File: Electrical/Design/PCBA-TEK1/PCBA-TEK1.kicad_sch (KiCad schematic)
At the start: 0 parts

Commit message: SUKU sync
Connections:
- no-connect marks 1 -> 11
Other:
- added sheet UI_DISPLAY (UI_DISPLAY.kicad_sch)
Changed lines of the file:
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@@
   (junction (at 213.36 185.42) (diameter 0) (color 0 0 0 0)
   )
+  (no_connect (at 208.28 147.32))
+  (no_connect (at 208.28 165.1))
+  (no_connect (at 208.28 157.48))
+  (no_connect (at 208.28 134.62))
+  (no_connect (at 208.28 160.02))
   (no_connect (at 208.28 111.76))
+  (no_connect (at 208.28 142.24))
+  (no_connect (at 208.28 137.16))
+  (no_connect (at 208.28 129.54))
+  (no_connect (at 208.28 139.7))
+  (no_connect (at 208.28 162.56))
   (wire (pts (xy 175.26 203.2) (xy 170.18 203.2))
     (stroke (width 0) (type default))
@@
     (stroke (width 0) (type default))
   )
+  (wire (pts (xy 203.2 147.32) (xy 208.28 147.32))
+    (stroke (width 0) (type default))
+  )
   (wire (pts (xy 175.26 198.12) (xy 170.18 198.12))
     (stroke (width 0) (type default))
@@
     (stroke (width 0) (type default))
   )
+  (wire (pts (xy 203.2 162.56) (xy 208.28 162.56))
+    (stroke (width 0) (type default))
+  )
   (wire (pts (xy 175.26 220.98) (xy 170.18 220.98))
     (stroke (width 0) (type default))
@@
     (stroke (width 0) (type default))
   )
+  (wire (pts (xy 203.2 129.54) (xy 208.28 129.54))
+    (stroke (width 0) (type default))
+  )
+  (wire (pts (xy 203.2 157.48) (xy 208.28 157.48))
+    (stroke (width 0) (type default))
+  )
+  (wire (pts (xy 203.2 134.62) (xy 208.28 134.62))
+    (stroke (width 0) (type default))
+  )
   (wire (pts (xy 175.26 193.04) (xy 170.18 193.04))
     (stroke (width 0) (type default))
@@
     (stroke (width 0) (type default))
   )
+  (wire (pts (xy 203.2 165.1) (xy 208.28 165.1))
+    (stroke (width 0) (type default))
+  )
   (wire (pts (xy 213.36 185.42) (xy 215.9 185.42))
     (stroke (width 0) (type default))
@@
     (stroke (width 0) (type default))
   )
+  (wire (pts (xy 203.2 142.24) (xy 208.28 142.24))
+    (stroke (width 0) (type default))
+  )
   (wire (pts (xy 215.9 187.96) (xy 213.36 187.96))
     (stroke (width 0) (type default))
@@
     (stroke (width 0) (type default))
   )
+  (wire (pts (xy 203.2 160.02) (xy 208.28 160.02))
+    (stroke (width 0) (type default))
+  )
+  (wire (pts (xy 203.2 139.7) (xy 208.28 139.7))
+    (stroke (width 0) (type default))
+  )
   (wire (pts (xy 200.66 198.12) (xy 215.9 198.12))
     (stroke (width 0) (type default))
   )
   (wire (pts (xy 127 193.04) (xy 132.08 193.04))
+    (stroke (width 0) (type default))
+  )
+  (wire (pts (xy 203.2 137.16) (xy 208.28 137.16))
     (stroke (width 0) (type default))
   )
@@
       )
     )
+  )
+  (sheet (at 177.8 127) (size 25.4 40.64) (fields_autoplaced)
+    (stroke (width 0.1524) (type solid))
+    (fill (color 0 0 0 0.0000))
+    (property "Sheetname" "UI_DISPLAY" (at 177.8 126.2884 0)
+      (effects (font (size 1.27 1.27)) (justify left bottom))
+    )
+    (property "Sheetfile" "UI_DISPLAY.kicad_sch" (at 177.8 168.2246 0)
+      (effects (font (size 1.27 1.27)) (justify left top))
+    )
+    (pin "~{RESET}" input (at 203.2 147.32 0)
+      (effects (font (size 1.27 1.27)) (justify right))
+    )
+    (pin "~{BACKLIGHT}" passive (at 203.2 129.54 0)
+      (effects (font (size 1.27 1.27)) (justify right))
+    )
+    (pin "~{CS}" input (at 203.2 134.62 0)
+      (effects (font (size 1.27 1.27)) (justify right))
+    )
+    (pin "D{slash}~{C}" input (at 203.2 137.16 0)
+      (effects (font (size 1.27 1.27)) (justify right))
+    )
+    (pin "SDIO" input (at 203.2 139.7 0)
+      (effects (font (size 1.27 1.27)) (justify right))
+    )
+    (pin "SCLK" input (at 203.2 142.24 0)
+      (effects (font (size 1.27 1.27)) (justify right))
+    )
+    (pin "BTN_1" output (at 203.2 160.02 0)
+      (effects (font (size 1.27 1.27)) (justify right))
+    )
+    (pin "BTN_0" output (at 203.2 157.48 0)
+      (effects (font (size 1.27 1.27)) (justify right))
+    )
+    (pin "BTN_3" output (at 203.2 162.56 0)
+      (effects (font (size 1.27 1.27)) (justify right))
+    )
+    (pin "BTN_2" output (at 203.2 165.1 0)
+      (effects (font (size 1.27 1.27)) (justify right))
+    )
+    (instances
+      (project "PCBA-TEK1"
+        (path "/e5217a0c-7f55-4c30-adda-7f8d95709d1b" (page "11"))
+      )
+    )

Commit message: SUKU layout finished
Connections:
- no-connect marks 11 -> 1
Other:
- sheet UI_POT renamed UI_POT_BTN
- sheet UI_DISPLAY ports: added none; removed BTN_0, BTN_1, BTN_2, BTN_3
- sheet UI_POT_BTN: file UI_POT.kicad_sch -> UI_POT_BTN.kicad_sch

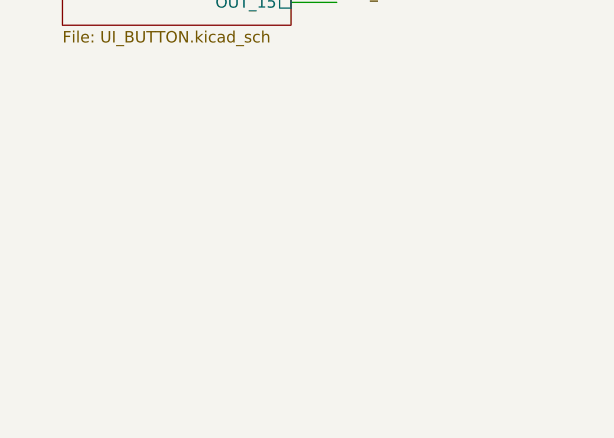
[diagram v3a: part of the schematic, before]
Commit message: SUKU interface connection added
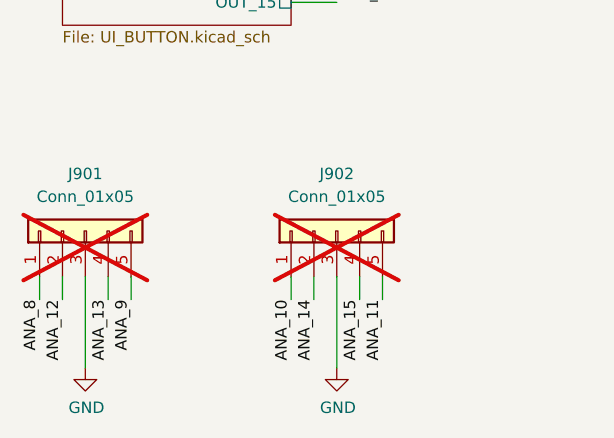
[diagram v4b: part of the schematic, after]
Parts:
- added J901, J902: Conn_01x05, Connector_PinHeader_2.54mm:PinHeader_1x05_P2.54mm_Vertical, symbol Connector_Generic:Conn_01x05
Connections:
- net ANA_10: now also J902.1 (Pin_1)
- net ANA_11: now also J902.5 (Pin_5)
- net ANA_12: now also J901.2 (Pin_2)
- net ANA_13: now also J901.4 (Pin_4)
- net ANA_14: now also J902.2 (Pin_2)
- net ANA_15: now also J902.4 (Pin_4)
- net ANA_8: now also J901.1 (Pin_1)
- net ANA_9: now also J901.5 (Pin_5)
- new net GND: J901.3 (Pin_3), J902.3 (Pin_3)
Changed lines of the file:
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@@
   )
   (no_connect (at 208.28 111.76))
+  (wire (pts (xy 137.16 233.68) (xy 137.16 236.22))
+    (stroke (width 0) (type default))
+  )
   (wire (pts (xy 175.26 203.2) (xy 170.18 203.2))
     (stroke (width 0) (type default))
@@
     (stroke (width 0) (type default))
   )
+  (wire (pts (xy 99.06 233.68) (xy 99.06 236.22))
+    (stroke (width 0) (type default))
+  )
   (wire (pts (xy 175.26 198.12) (xy 170.18 198.12))
     (stroke (width 0) (type default))
@@
     (stroke (width 0) (type default))
   )
+  (wire (pts (xy 127 233.68) (xy 127 236.22))
+    (stroke (width 0) (type default))
+  )
   (wire (pts (xy 127 119.38) (xy 132.08 119.38))
     (stroke (width 0) (type default))
   )
+  (wire (pts (xy 106.68 233.68) (xy 106.68 236.22))
+    (stroke (width 0) (type default))
+  )
   (wire (pts (xy 132.08 195.58) (xy 127 195.58))
     (stroke (width 0) (type default))
@@
     (stroke (width 0) (type default))
   )
+  (wire (pts (xy 134.62 233.68) (xy 134.62 236.22))
+    (stroke (width 0) (type default))
+  )
+  (wire (pts (xy 104.14 233.68) (xy 104.14 243.84))
+    (stroke (width 0) (type default))
+  )
   (wire (pts (xy 200.66 228.6) (xy 215.9 228.6))
     (stroke (width 0) (type default))
@@
     (stroke (width 0) (type default))
   )
+  (wire (pts (xy 101.6 233.68) (xy 101.6 236.22))
+    (stroke (width 0) (type default))
+  )
   (wire (pts (xy 175.26 218.44) (xy 170.18 218.44))
     (stroke (width 0) (type default))
@@
     (stroke (width 0) (type default))
   )
+  (wire (pts (xy 129.54 233.68) (xy 129.54 236.22))
+    (stroke (width 0) (type default))
+  )
   (wire (pts (xy 213.36 187.96) (xy 213.36 185.42))
     (stroke (width 0) (type default))
@@
     (stroke (width 0) (type default))
   )
+  (wire (pts (xy 132.08 243.84) (xy 132.08 233.68))
+    (stroke (width 0) (type default))
+  )
   (wire (pts (xy 175.26 228.6) (xy 170.18 228.6))
     (stroke (width 0) (type default))
@@
   )
   (wire (pts (xy 132.08 185.42) (xy 127 185.42))
+    (stroke (width 0) (type default))
+  )
+  (wire (pts (xy 109.22 233.68) (xy 109.22 236.22))
     (stroke (width 0) (type default))
   )
@@
     (effects (font (size 1.27 1.27)) (justify left bottom))
   )
+  (label "ANA_15" (at 134.62 236.22 270) (fields_autoplaced)
+    (effects (font (size 1.27 1.27)) (justify right bottom))
+  )
   (label "ANA_6" (at 132.08 116.84 0) (fields_autoplaced)
     (effects (font (size 1.27 1.27)) (justify left bottom))
@@
     (effects (font (size 1.27 1.27)) (justify right bottom))
   )
+  (label "ANA_13" (at 106.68 236.22 270) (fields_autoplaced)
+    (effects (font (size 1.27 1.27)) (justify right bottom))
+  )
   (label "ANA_9" (at 132.08 187.96 0) (fields_autoplaced)
     (effects (font (size 1.27 1.27)) (justify left bottom))
@@
     (effects (font (size 1.27 1.27)) (justify right bottom))
   )
+  (label "ANA_12" (at 101.6 236.22 270) (fields_autoplaced)
+    (effects (font (size 1.27 1.27)) (justify right bottom))
+  )
+  (label "ANA_9" (at 109.22 236.22 270) (fields_autoplaced)
+    (effects (font (size 1.27 1.27)) (justify right bottom))
+  )
   (label "ANA_7" (at 170.18 223.52 180) (fields_autoplaced)
     (effects (font (size 1.27 1.27)) (justify right bottom))
   )
+  (label "ANA_14" (at 129.54 236.22 270) (fields_autoplaced)
+    (effects (font (size 1.27 1.27)) (justify right bottom))
+  )
   (label "ANA_2" (at 170.18 215.9 180) (fields_autoplaced)
     (effects (font (size 1.27 1.27)) (justify right bottom))
@@
     (effects (font (size 1.27 1.27)) (justify left bottom))
   )
+  (label "ANA_11" (at 137.16 236.22 270) (fields_autoplaced)
+    (effects (font (size 1.27 1.27)) (justify right bottom))
+  )
+  (label "ANA_8" (at 99.06 236.22 270) (fields_autoplaced)
+    (effects (font (size 1.27 1.27)) (justify right bottom))
+  )
   (label "ANA_13" (at 132.08 198.12 0) (fields_autoplaced)
     (effects (font (size 1.27 1.27)) (justify left bottom))
@@
     (effects (font (size 1.27 1.27)) (justify right bottom))
   )
+  (label "ANA_10" (at 127 236.22 270) (fields_autoplaced)
+    (effects (font (size 1.27 1.27)) (justify right bottom))
+  )
   (label "ANA_0" (at 132.08 101.6 0) (fields_autoplaced)
     (effects (font (size 1.27 1.27)) (justify left bottom))
@@
     )
   )
+  (symbol (lib_id "power:GND") (at 104.14 243.84 0) (unit 1)
+    (in_bom yes) (on_board yes) (dnp no)
+    (property "Reference" "#PWR01006" (at 104.14 250.19 0)
+      (effects (font (size 1.27 1.27)) hide)
+    )
+    (property "Value" "GND" (at 104.267 248.2342 0)
+      (effects (font (size 1.27 1.27)))
+    )
+    (property "Footprint" "" (at 104.14 243.84 0)
+      (effects (font (size 1.27 1.27)) hide)
+    )
+    (property "Datasheet" "" (at 104.14 243.84 0)
+      (effects (font (size 1.27 1.27)) hide)
+    )
+    (pin "1")
+    (instances
+      (project "PCBA-TEK1"
+        (path "/e5217a0c-7f55-4c30-adda-7f8d95709d1b/00000000-0000-0000-0000-00005d7c8bfe"
+          (reference "#PWR01006") (unit 1)
+        )
+        (path "/e5217a0c-7f55-4c30-adda-7f8d95709d1b/00000000-0000-0000-0000-00005d8763e1"
+          (reference "#PWR01018") (unit 1)
+        )
+        (path "/e5217a0c-7f55-4c30-adda-7f8d95709d1b"
+          (reference "#PWR0963") (unit 1)
+        )
+      )
+    )
+  )
+  (symbol (lib_id "Connector_Generic:Conn_01x05") (at 104.14 228.6 90) (unit 1)
+    (in_bom yes) (on_board yes) (dnp yes) (fields_autoplaced)
+    (property "Reference" "J901" (at 104.14 222.25 90)
+      (effects (font (size 1.27 1.27)))
+    )
+    (property "Value" "Conn_01x05" (at 104.14 224.79 90)
+      (effects (font (size 1.27 1.27)))
+    )
+    (property "Footprint" "Connector_PinHeader_2.54mm:PinHeader_1x05_P2.54mm_Vertical" (at 104.14 228.6 0)
+      (effects (font (size 1.27 1.27)) hide)
+    )
+    (property "Datasheet" "~" (at 104.14 228.6 0)
+      (effects (font (size 1.27 1.27)) hide)
+    )
+    (pin "1")
+    (pin "2")
+    (pin "3")
+    (pin "4")
+    (pin "5")
+    (instances
+      (project "PCBA-TEK1"
+        (path "/e5217a0c-7f55-4c30-adda-7f8d95709d1b"
+          (reference "J901") (unit 1)
+        )
+      )
+    )
+  )
+  (symbol (lib_id "Connector_Generic:Conn_01x05") (at 132.08 228.6 90) (unit 1)
+    (in_bom yes) (on_board yes) (dnp yes) (fields_autoplaced)
+    (property "Reference" "J902" (at 132.08 222.25 90)
+      (effects (font (size 1.27 1.27)))
+    )
+    (property "Value" "Conn_01x05" (at 132.08 224.79 90)
+      (effects (font (size 1.27 1.27)))
+    )
+    (property "Footprint" "Connector_PinHeader_2.54mm:PinHeader_1x05_P2.54mm_Vertical" (at 132.08 228.6 0)
+      (effects (font (size 1.27 1.27)) hide)
+    )
+    (property "Datasheet" "~" (at 132.08 228.6 0)
+      (effects (font (size 1.27 1.27)) hide)
+    )
+    (pin "1")
+    (pin "2")
+    (pin "3")
+    (pin "4")
+    (pin "5")
+    (instances
+      (project "PCBA-TEK1"
+        (path "/e5217a0c-7f55-4c30-adda-7f8d95709d1b"
+          (reference "J902") (unit 1)
+        )
+      )
+    )
+  )
+  (symbol (lib_id "power:GND") (at 132.08 243.84 0) (unit 1)
+    (in_bom yes) (on_board yes) (dnp no)
+    (property "Reference" "#PWR01006" (at 132.08 250.19 0)
+      (effects (font (size 1.27 1.27)) hide)
+    )
+    (property "Value" "GND" (at 132.207 248.2342 0)
+      (effects (font (size 1.27 1.27)))
+    )
+    (property "Footprint" "" (at 132.08 243.84 0)
+      (effects (font (size 1.27 1.27)) hide)
+    )
+    (property "Datasheet" "" (at 132.08 243.84 0)
+      (effects (font (size 1.27 1.27)) hide)
+    )
+    (pin "1")
+    (instances
+      (project "PCBA-TEK1"
+        (path "/e5217a0c-7f55-4c30-adda-7f8d95709d1b/00000000-0000-0000-0000-00005d7c8bfe"
+          (reference "#PWR01006") (unit 1)
+        )
+        (path "/e5217a0c-7f55-4c30-adda-7f8d95709d1b/00000000-0000-0000-0000-00005d8763e1"
+          (reference "#PWR01018") (unit 1)
+        )
+        (path "/e5217a0c-7f55-4c30-adda-7f8d95709d1b"
+          (reference "#PWR0978") (unit 1)
+        )
+      )
+    )
+  )

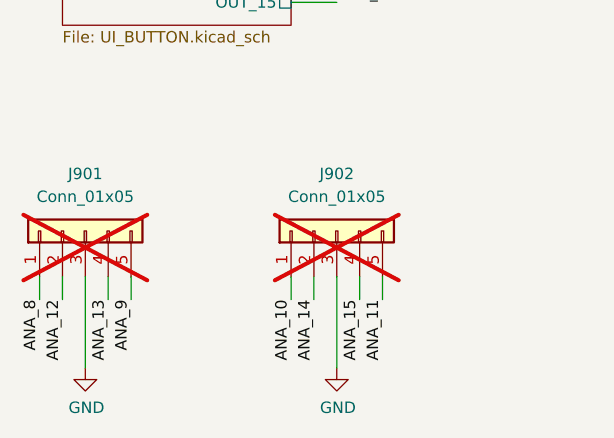
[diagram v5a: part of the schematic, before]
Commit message: SUKU TEK1 omron switches removed, cutout added for switch sockets
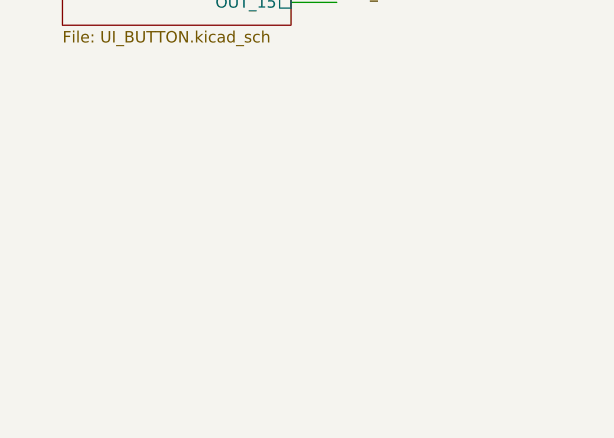
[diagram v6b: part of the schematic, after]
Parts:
- removed J901, J902: Conn_01x05, Connector_PinHeader_2.54mm:PinHeader_1x05_P2.54mm_Vertical, symbol Connector_Generic:Conn_01x05
